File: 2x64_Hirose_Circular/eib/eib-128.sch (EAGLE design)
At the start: 36 parts

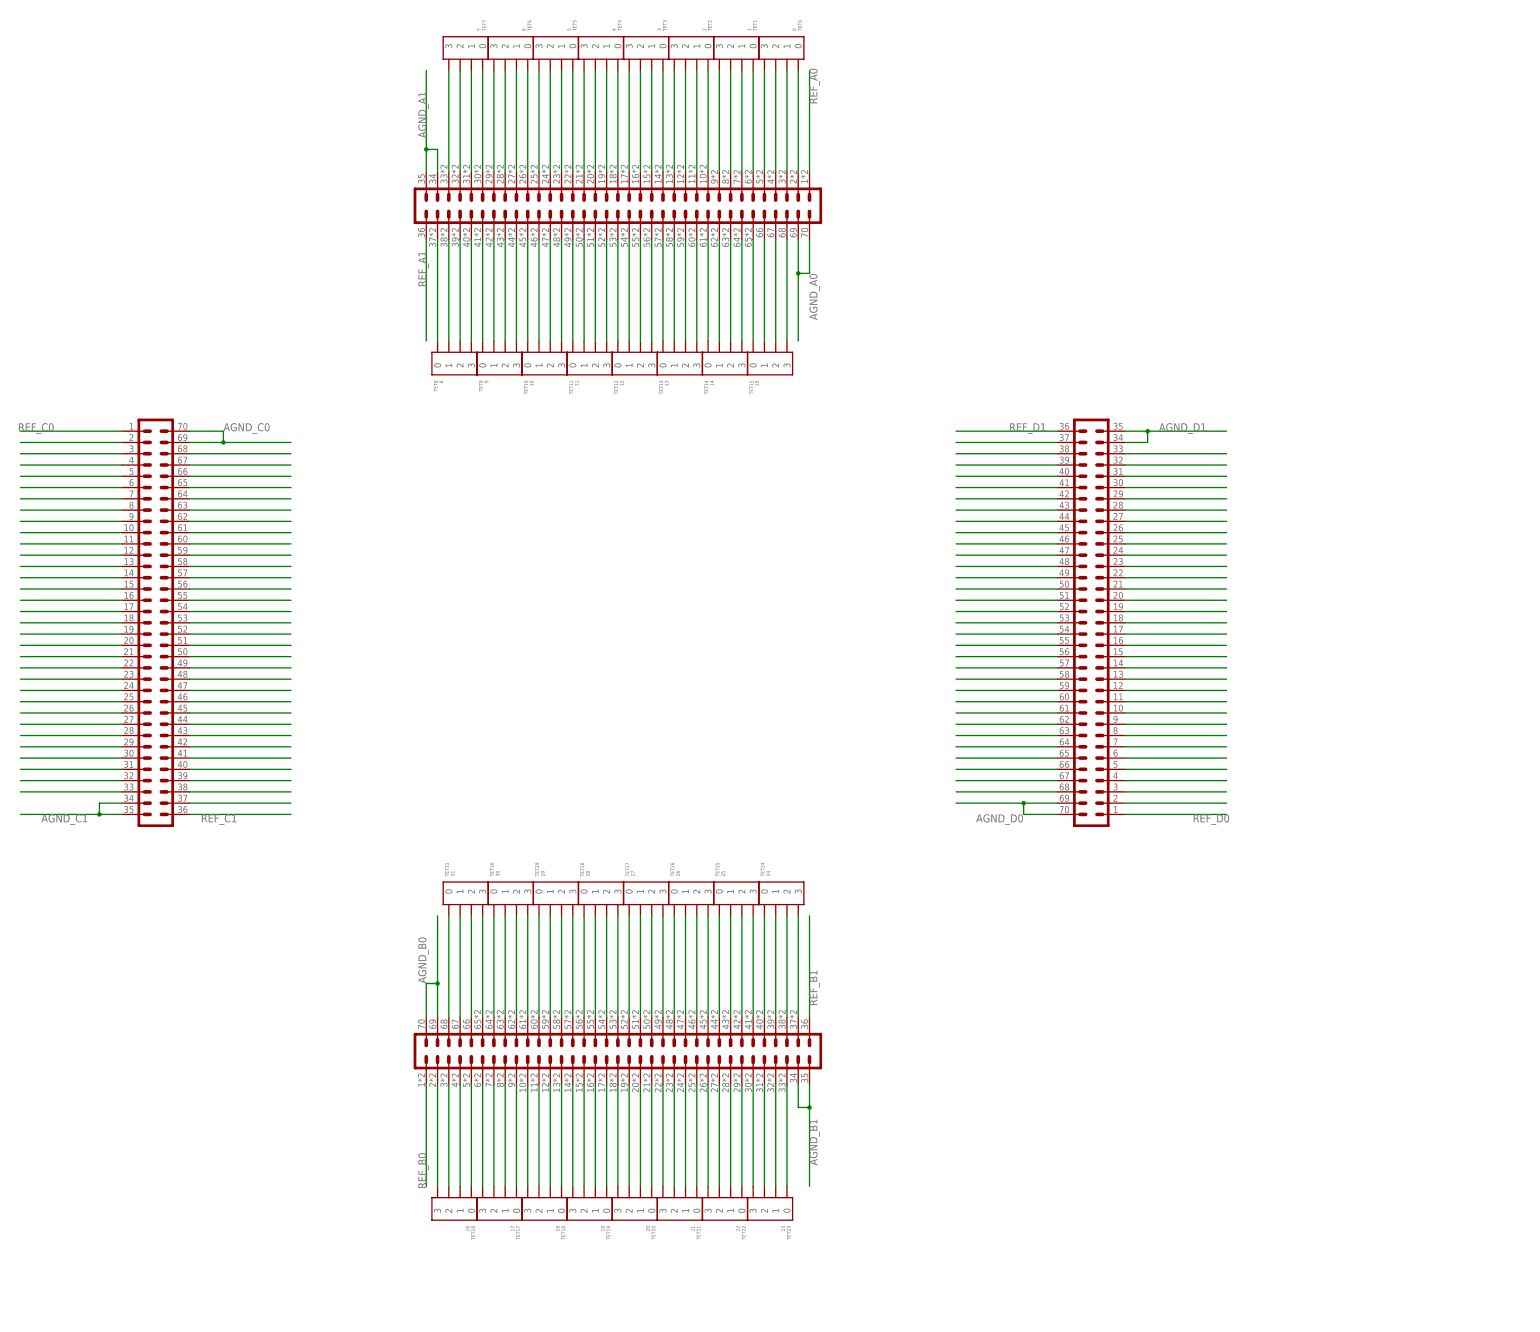
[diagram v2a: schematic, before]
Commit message: Nearly finished with 128-channel EIB
Still need to really figure out the reference/ground/sheild situation. I
want to make these as jumperable and reconfigurable as possible.
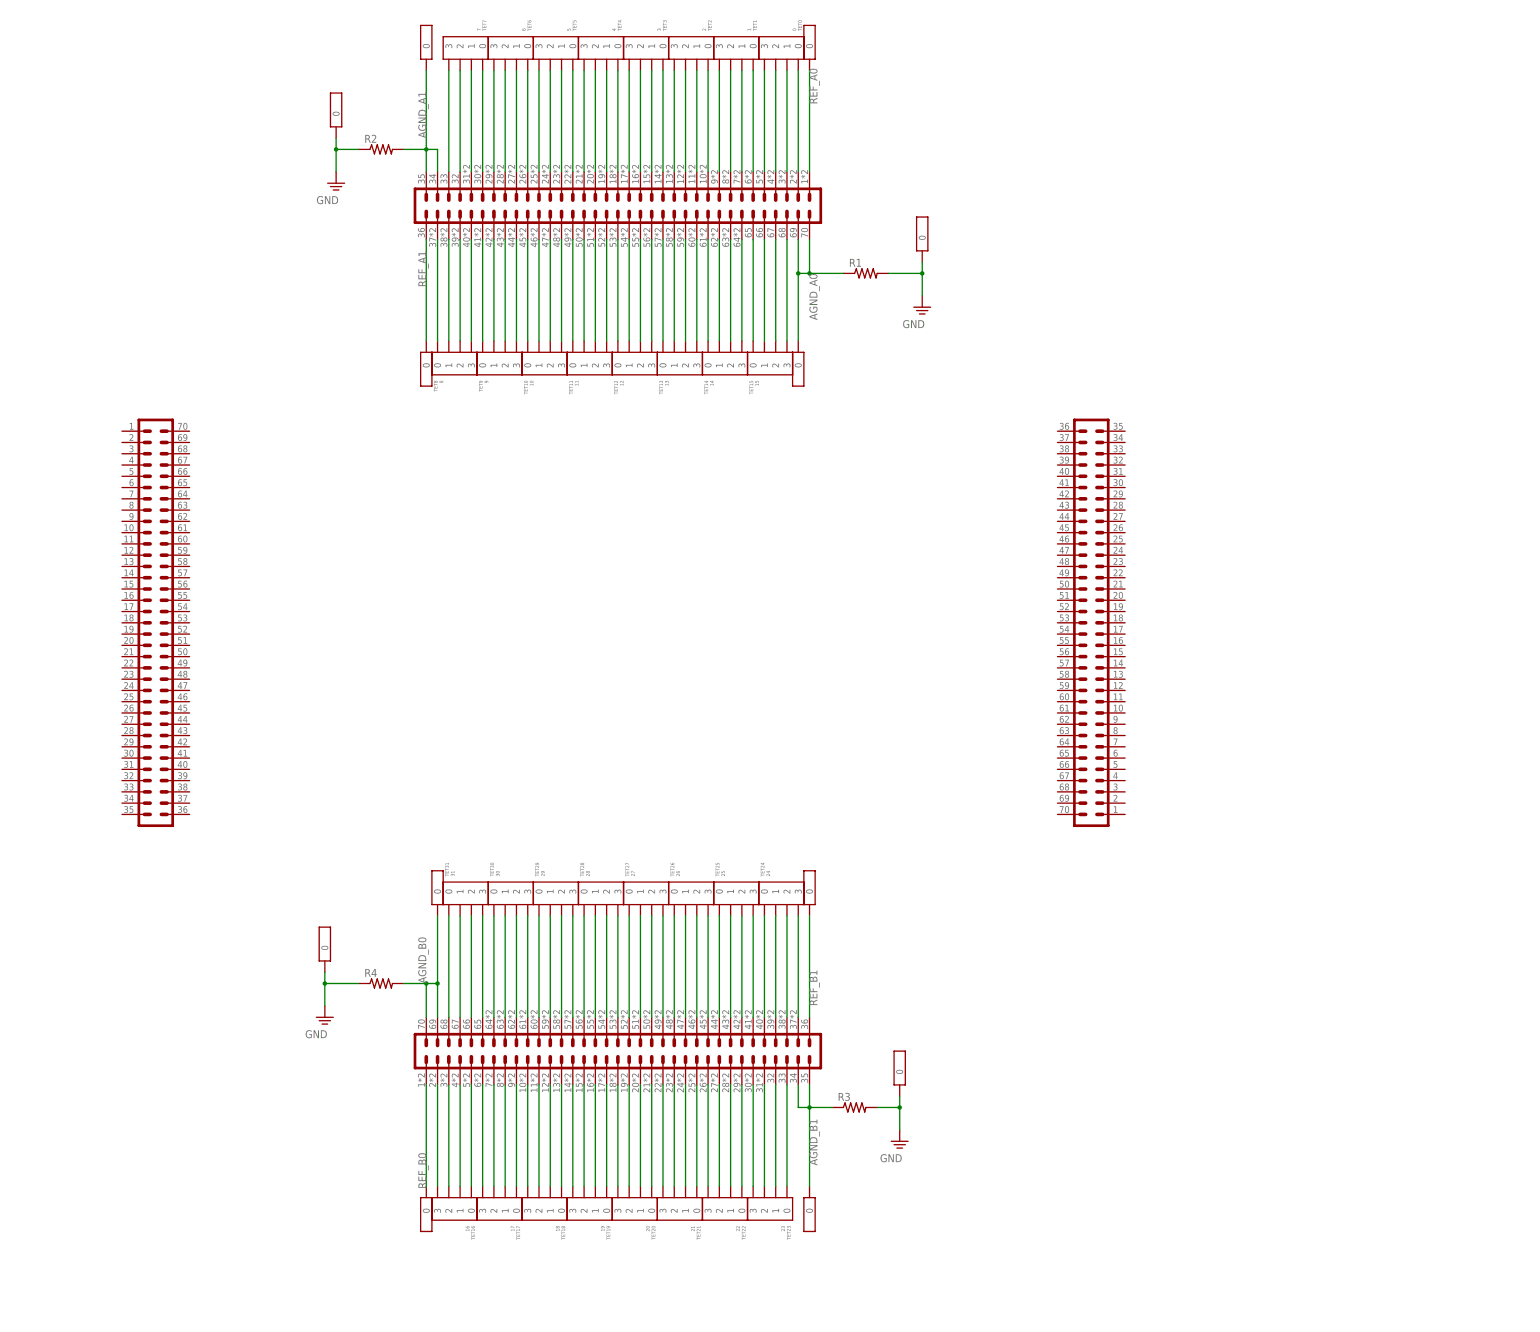
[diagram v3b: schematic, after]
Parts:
- added AGND_A0, AGND_A1, REF_A0, REF_A1, SHA0, SHA1, SHB0, SHB1, U$5, U$6, U$7, U$8: GOLDPIN_0.5ID_0.7OD, jonnew:GOLDPIN_0.5ID_0.7OD
- added R1, R2, R3, R4: (no value), jonnew:R_0201
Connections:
- removed net AGND_C0: C.69, C.70
- removed net AGND_C1: C.34, C.35
- removed net AGND_D0: D.69, D.70
- removed net AGND_D1: D.34, D.35
- removed net N$1: D.33
- removed net N$10: D.24
- removed net N$11: D.23
- removed net N$12: D.22
- removed net N$129: C.33
- removed net N$13: D.21
- removed net N$130: C.32
- removed net N$131: C.31
- removed net N$132: C.30
- removed net N$133: C.29
- removed net N$134: C.28
- removed net N$135: C.27
- removed net N$136: C.26
- removed net N$137: C.25
- removed net N$138: C.24
- removed net N$139: C.23
- removed net N$14: D.20
- removed net N$140: C.22
- removed net N$141: C.21
- removed net N$142: C.20
- removed net N$143: C.19
- removed net N$144: C.18
- removed net N$145: C.17
- removed net N$146: C.16
- removed net N$147: C.15
- removed net N$148: C.14
- removed net N$149: C.13
- removed net N$15: D.19
- removed net N$150: C.12
- removed net N$151: C.11
- removed net N$152: C.10
- removed net N$153: C.9
- removed net N$154: C.8
- removed net N$155: C.7
- removed net N$156: C.6
- removed net N$157: C.5
- removed net N$158: C.4
- removed net N$159: C.3
- removed net N$16: D.18
- removed net N$160: C.38
- removed net N$161: C.39
- removed net N$162: C.40
- removed net N$163: C.41
- removed net N$164: C.42
- removed net N$165: C.43
- removed net N$166: C.44
- removed net N$167: C.45
- removed net N$168: C.46
- removed net N$169: C.47
- removed net N$17: D.17
- removed net N$170: C.48
- removed net N$171: C.49
- removed net N$172: C.50
- removed net N$173: C.51
- removed net N$174: C.52
- removed net N$175: C.53
- removed net N$176: C.54
- removed net N$177: C.55
- removed net N$178: C.56
- removed net N$179: C.57
- removed net N$18: D.16
- removed net N$180: C.58
- removed net N$181: C.59
- removed net N$182: C.60
- removed net N$183: C.61
- removed net N$184: C.62
- removed net N$185: C.63
- removed net N$186: C.64
- removed net N$187: C.65
- removed net N$188: C.66
- removed net N$189: C.67
- removed net N$19: D.15
- removed net N$190: C.68
- removed net N$191: C.2
- removed net N$192: C.37
- removed net N$2: D.32
- removed net N$20: D.14
- removed net N$21: D.13
- removed net N$22: D.12
- removed net N$23: D.11
- removed net N$24: D.10
- removed net N$25: D.9
- removed net N$26: D.8
- removed net N$27: D.7
- removed net N$28: D.6
- removed net N$29: D.5
- removed net N$3: D.31
- removed net N$30: D.4
- removed net N$31: D.3
- removed net N$32: D.38
- removed net N$33: D.39
- removed net N$34: D.40
- removed net N$35: D.41
- removed net N$36: D.42
- removed net N$37: D.43
- removed net N$38: D.44
- removed net N$39: D.45
- removed net N$4: D.30
- removed net N$40: D.46
- removed net N$41: D.47
- removed net N$42: D.48
- removed net N$43: D.49
- removed net N$44: D.50
- removed net N$45: D.51
- removed net N$46: D.52
- removed net N$47: D.53
- removed net N$48: D.54
- removed net N$49: D.55
- removed net N$5: D.29
- removed net N$50: D.56
- removed net N$51: D.57
- removed net N$52: D.58
- removed net N$53: D.59
- removed net N$54: D.60
- removed net N$55: D.61
- removed net N$56: D.62
- removed net N$57: D.63
- removed net N$58: D.64
- removed net N$59: D.65
- removed net N$6: D.28
- removed net N$60: D.66
- removed net N$61: D.67
- removed net N$62: D.68
- removed net N$63: D.2
- removed net N$64: D.37
- removed net N$7: D.27
- removed net N$8: D.26
- removed net N$9: D.25
- removed net REF_C0: C.1
- removed net REF_C1: C.36
- removed net REF_D0: D.1
- removed net REF_D1: D.36
- new net GND: R1.2, R2.1, R3.2, R4.1, SHA0.0, SHA1.0, SHB0.0, SHB1.0
- net AGND_A0: now also AGND_A0.0, R1.1
- net AGND_A1: now also AGND_A1.0, R2.2
- net AGND_B0: now also R4.2, U$5.0
- net AGND_B1: now also R3.1, U$7.0
- net REF_A0: now also REF_A0.0
- net REF_A1: now also REF_A1.0
- net REF_B0: now also U$8.0
- net REF_B1: now also U$6.0

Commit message: More 128 channel EIB routing.
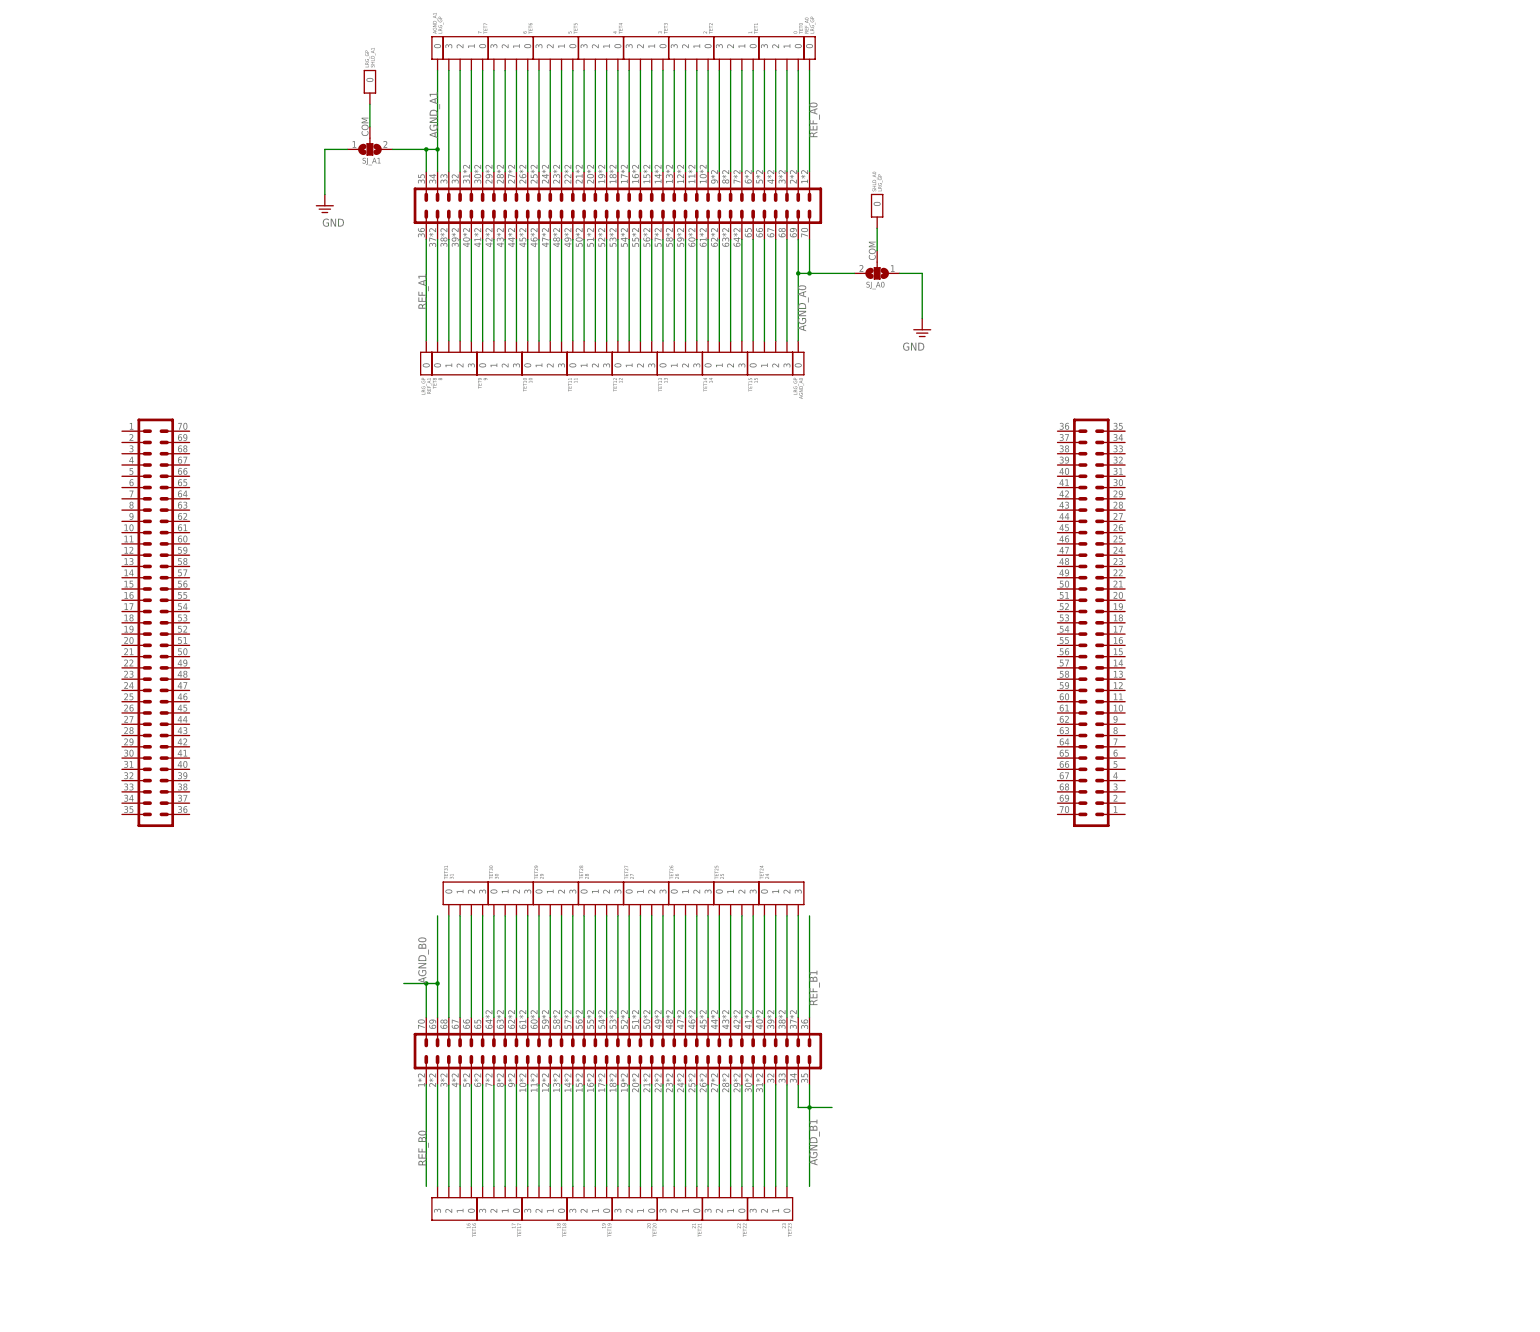
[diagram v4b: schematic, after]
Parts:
- removed R1, R2, R3, R4: (no value), jonnew:R_0201
- removed SHA0, SHA1, SHB0, SHB1, U$5, U$6, U$7, U$8: GOLDPIN_0.5ID_0.7OD, jonnew:GOLDPIN_0.5ID_0.7OD
- added SHLD_A0, SHLD_A1: LRG_GP, jonnew:GOLDPIN_0.5ID_0.7OD
- added SJ_A0, SJ_A1: (no value), jonnew:SJ2_0201
- AGND_A0, AGND_A1, REF_A0, REF_A1: value GOLDPIN_0.5ID_0.7OD -> LRG_GP
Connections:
- new net N$1: SHLD_A0.0, SJ_A0.COM
- new net N$2: SHLD_A1.0, SJ_A1.COM
- net AGND_A0: now also SJ_A0.2; no longer R1.1
- net AGND_A1: now also SJ_A1.2; no longer R2.2
- net AGND_B0: no longer R4.2, U$5.0
- net AGND_B1: no longer R3.1, U$7.0
- net GND: now also SJ_A0.1, SJ_A1.1; no longer R1.2, R2.1, R3.2, R4.1, SHA0.0, SHA1.0, SHB0.0, SHB1.0
- net REF_B0: no longer U$8.0
- net REF_B1: no longer U$6.0

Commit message: Finished laying out 128 channel EIB. Need to make cheap prototypes to make sure mech properties are good.
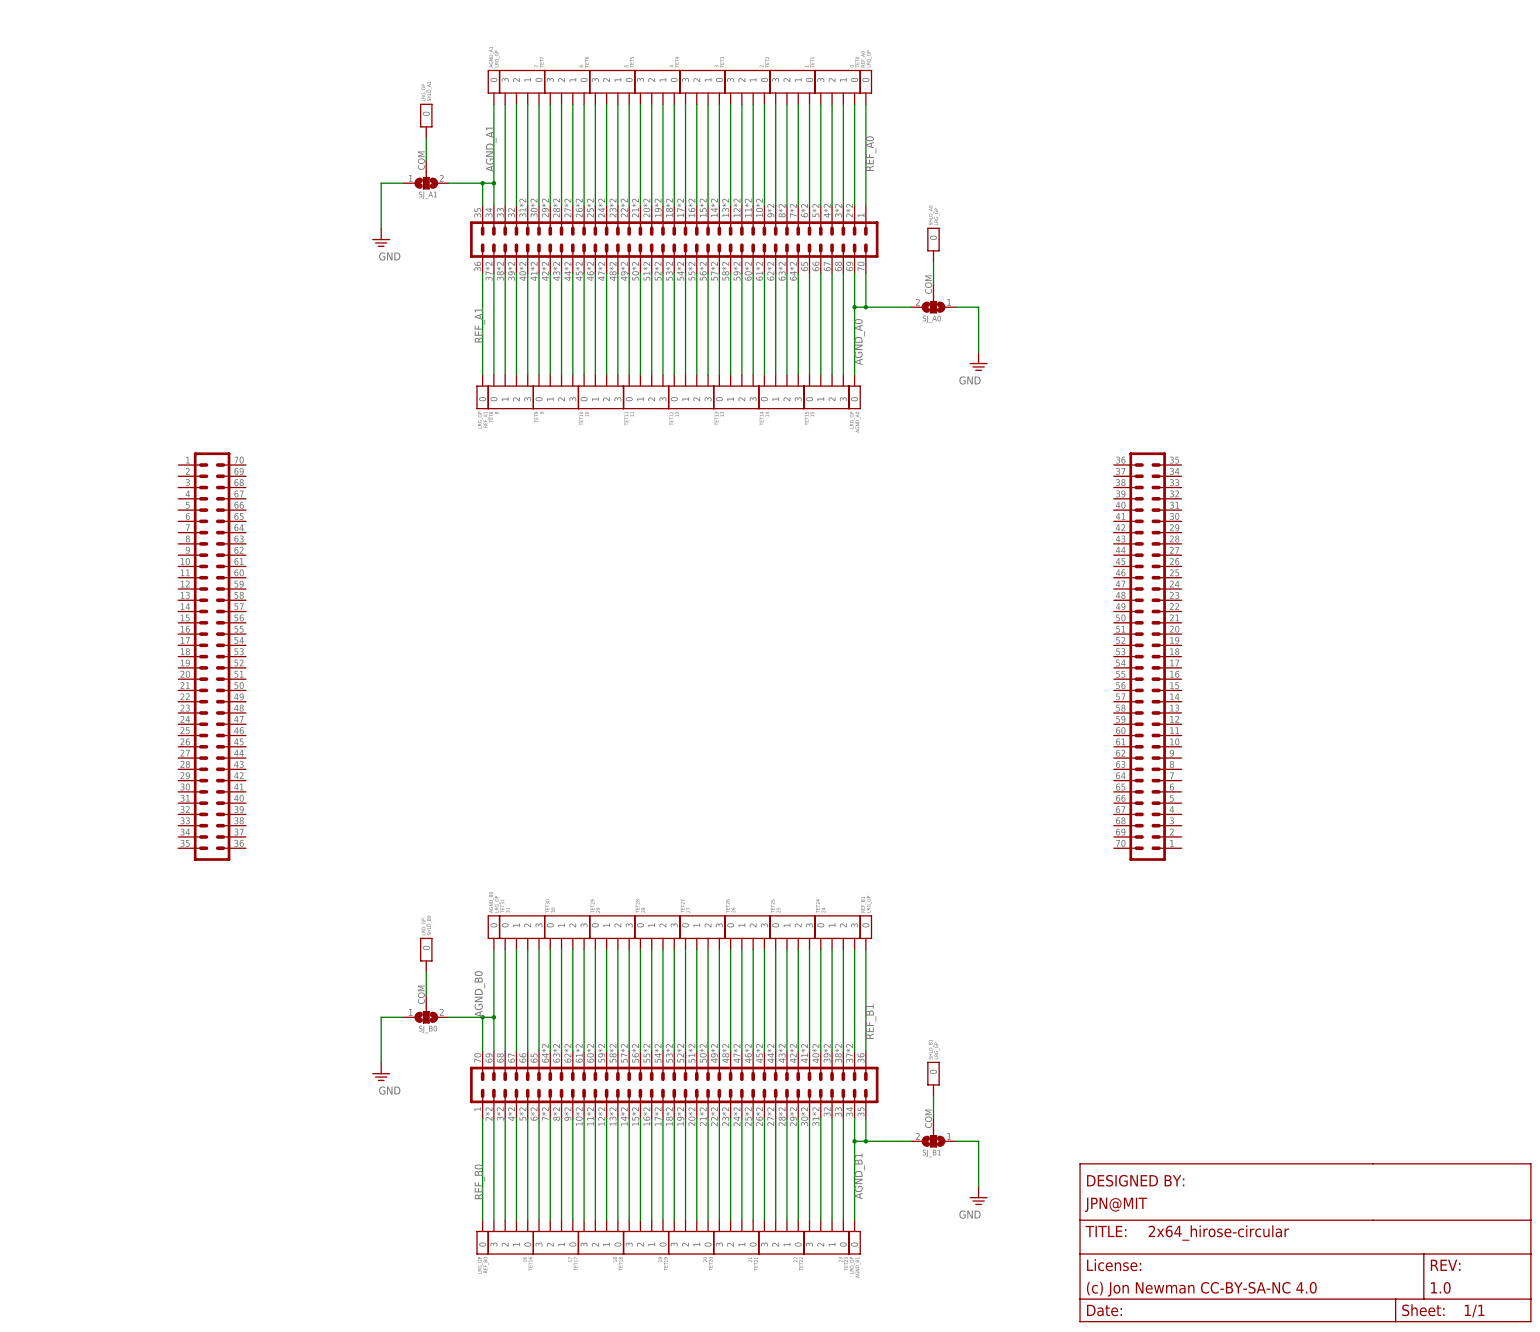
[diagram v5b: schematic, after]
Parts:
- added AGND_B0, AGND_B1, REF_B0, REF_B1, SHLD_B0, SHLD_B1: LRG_GP, jonnew:GOLDPIN_0.5ID_0.7OD
- added SJ_B0, SJ_B1: (no value), jonnew:SJ2_0201
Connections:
- new net N$3: SHLD_B0.0, SJ_B0.COM
- new net N$4: SHLD_B1.0, SJ_B1.COM
- net AGND_B0: now also AGND_B0.0, SJ_B0.2
- net AGND_B1: now also AGND_B1.0, SJ_B1.2
- net GND: now also SJ_B0.1, SJ_B1.1
- net REF_B0: now also REF_B0.0
- net REF_B1: now also REF_B1.0
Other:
- moved on the sheet: AGND_A0, AGND_A1, REF_A0, REF_A1, SHLD_A0, SHLD_A1, SJ_A0, SJ_A1, TET0, TET1, TET10, TET11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

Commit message: Finished 128-channel spi interface. Time to fabricate mechanical mockups.
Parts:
- renumbered A to AIN_N0T, B to AIN_S0T, C to MECH_W0T, D to MECH_E0T
